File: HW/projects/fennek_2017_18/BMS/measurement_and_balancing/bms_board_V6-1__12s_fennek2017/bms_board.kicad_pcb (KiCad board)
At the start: 4 copper layers, 55 x 48.5 mm, 200 parts, among them IC1 TI-bq76pl536, IC2 TI-bq76pl536, P1 Battery_Interface, P2 TS1, P3 TS2, P4 Host_Interface, Q1 BSS205N, Q10 BSS205N, Q11 BSS205N, Q12 BSS205N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

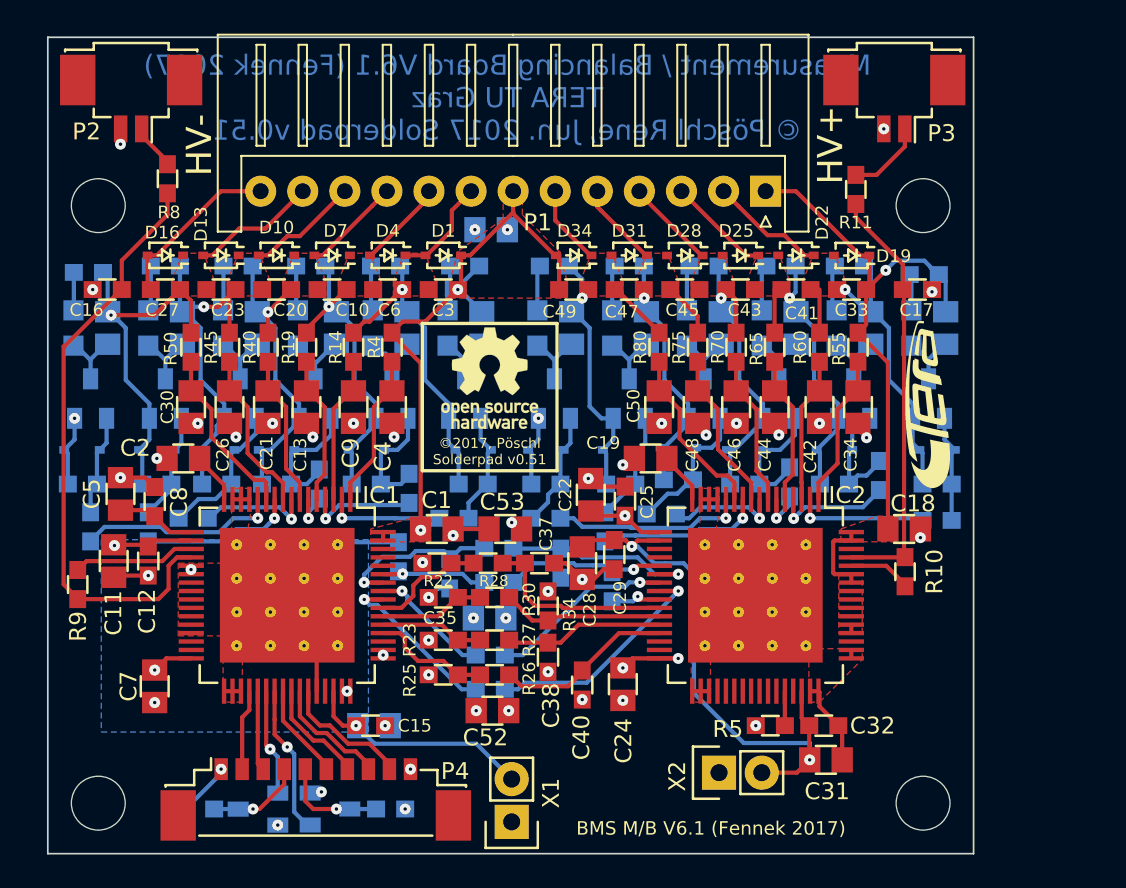
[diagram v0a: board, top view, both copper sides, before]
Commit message: Update github repo with designs for fennek 2018
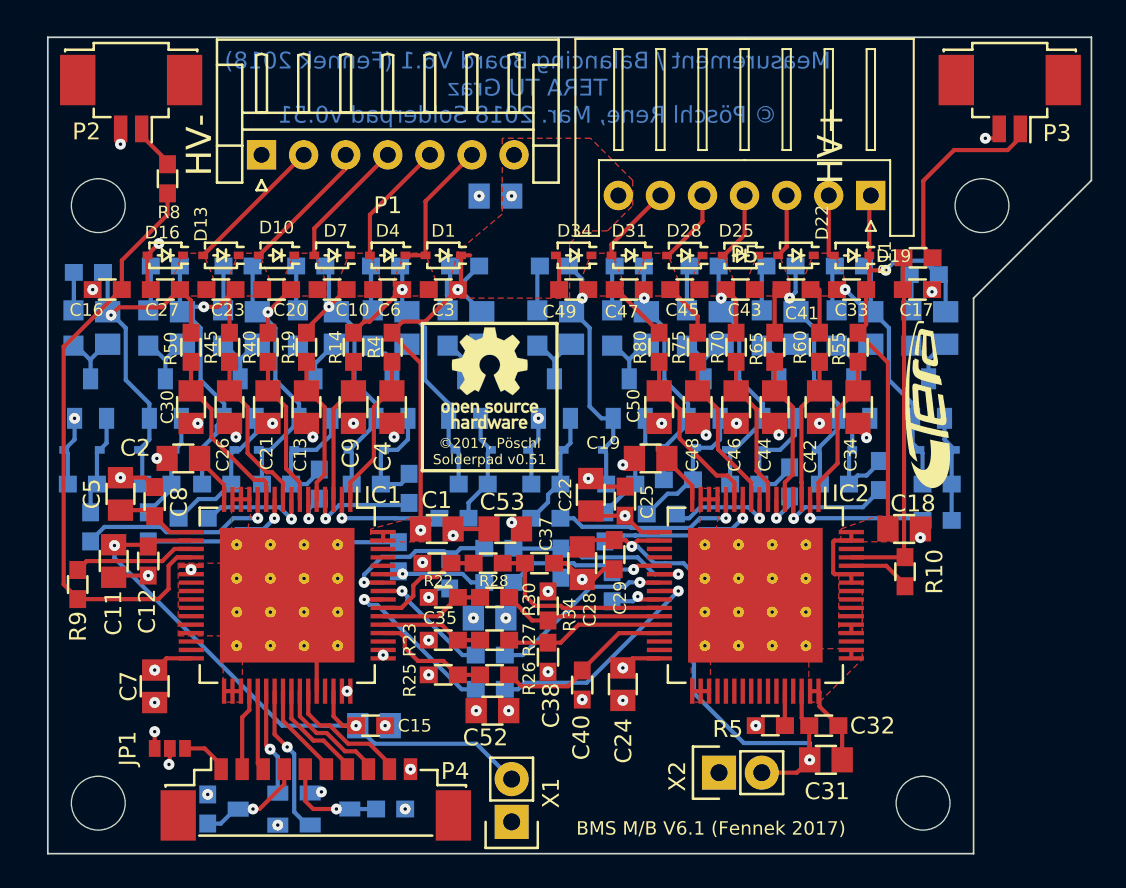
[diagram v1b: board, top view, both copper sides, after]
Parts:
- added JP1: JUMPER3_NO, tera_general:SOLDERJUMPER_3_1mm, F.Cu at (87.9, 146.4)
- added P5: CONN_01X07, tera_Connectors_JST:JST_XH_S07B-XH-A_07x2.50mm_Angled, F.Cu at (129.5, 113.5)
- P1: value Battery_Interface -> CONN_01X07; footprint tera_Connectors_JST:JST_XH_S13B-XH-A_13x2.50mm_Angled -> tera_Connectors_JST:JST_EH_S07B-EH_07x2.50mm_Angled
- moved P1 30.0 mm to (93.3, 111.1), turned to 0 degrees
- moved P3 6.86 mm to (137.8, 106.7)
- moved R11 5.49 mm to (132.3, 117.2), turned to 0 degrees
- moved REF** 3.50 mm to (136.1, 114.1)
- moved C51 2.02 mm to (107.2, 113.6)
- moved R36 0.48 mm to (90.1, 150.0), turned to 270 degrees
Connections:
- P1 pad 1: +BATT -> GND
- P1 pad 2: /Chip2/VC5 -> /Chip1/VC1
- P1 pad 3: /Chip2/VC4 -> /Chip1/VC2
- P1 pad 4: /Chip2/VC3 -> /Chip1/VC3
- P1 pad 5: /Chip2/VC2 -> /Chip1/VC4
- P1 pad 6: /Chip2/VC1 -> /Chip1/VC5
- R36 pad 1: /Host_connect/+5V_Host -> /Host_connect/+5V_DO
- R37 pad 1: /Host_connect/+5V_Host -> /Host_connect/+5V_DO
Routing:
- net /Chip1/LDODx: track 18.3 -> 37.5 mm
- net Vmiddle: track 68.0 -> 59.3 mm
- net Net-(P3-Pad1): track 4.66 -> 12.1 mm
- net GND: track 36.2 -> 28.8 mm, vias 25 -> 26
- net +BATT: track 39.0 -> 34.4 mm
- net /Chip2/TS2+: track 25.4 -> 21.0 mm
- net /Chip2/VC5: track 26.5 -> 23.1 mm
- net /Chip2/VC4: track 24.4 -> 22.0 mm
- net /Chip1/VC4: track 23.4 -> 25.6 mm
- net /Chip1/VC5: track 24.4 -> 26.6 mm
- net /Chip1/VC3: track 25.3 -> 27.2 mm
- net /Chip1/VC2: track 28.0 -> 29.4 mm
- net /Chip2/VC3: track 24.2 -> 23.0 mm
- net +5V: track 3.38 -> 4.38 mm, vias 3 -> 4
- net /Host_connect/+5V_DO: track 0.00 -> 0.97 mm, vias 0 -> 3
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- added copper zone on In2.Cu, net /Host_connect/+5V_DO
- removed copper zone on B.Cu, net /Chip1/LDODx
- removed copper zone on In2.Cu, net /Host_connect/+5V_Host
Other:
- board size 55 x 48.5 mm -> 62 x 48.5 mm
- board text added: "Measurement / Balancing Board V6.1 (Fennek 2018) TERA TU Graz © Pöschl Rene, Mar. 2018 Solderpad v0.51"
- board text removed: "Measurement / Balancing Board V6.1 (Fennek 2017) TERA TU Graz © Pöschl Rene, Jun. 2017 Solderpad v0.51"
